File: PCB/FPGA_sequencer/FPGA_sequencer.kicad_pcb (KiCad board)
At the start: 2 copper layers, 19 parts, among them U1 ADA4940-2ACPZ-R7_a, U2 AD9648BCPZ-125, U3 DB3S406F0L, U4 DB3S406F0L

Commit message: pass capacitor add
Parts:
- added 10n1: 0.1u, Capacitors_SMD:C_0603, F.Cu at (97.8, 13.7)
- added C10: 0.1u, Capacitors_SMD:C_0603, F.Cu at (105.5, 16.1)
- added C11: 0.1u, Capacitors_SMD:C_0603, F.Cu at (109.3, 13.7)
- added C12: 0.1u, Capacitors_SMD:C_0603, F.Cu at (101.6, 20.8)
- added C13: 10n, Capacitors_SMD:C_0603, F.Cu at (105.5, 18.4)
- added C14: 10n, Capacitors_SMD:C_0603, F.Cu at (109.3, 16.1)
- added C15: 10n, Capacitors_SMD:C_0603, F.Cu at (105.5, 20.8)
- added C3: 10u, Capacitors_SMD:C_0603, F.Cu at (97.8, 16.1)
- added C4: 10u, Capacitors_SMD:C_0603, F.Cu at (101.6, 13.7)
- added C5: 1u, Capacitors_SMD:C_0603, F.Cu at (97.8, 18.4)
- added C6: 1u, Capacitors_SMD:C_0603, F.Cu at (101.6, 16.1)
- added C7: 0.1u, Capacitors_SMD:C_0603, F.Cu at (105.5, 13.7)
- added C8: 0.1u, Capacitors_SMD:C_0603, F.Cu at (97.8, 20.8)
- added C9: 0.1u, Capacitors_SMD:C_0603, F.Cu at (101.6, 18.4)
- C1, C2: footprint Capacitor_SMD:C_0603_1608Metric -> Capacitors_SMD:C_0603
- moved U2 9.48 mm to (134.1, 33.0)
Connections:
- U1 pad 10: Net-(U1-Pad10) -> Net-(C11-Pad2)
- U1 pad 15: Net-(U1-Pad15) -> Net-(10n1-Pad1)
- U1 pad 16: Net-(U1-Pad16) -> Net-(10n1-Pad1)
- U1 pad 22: Net-(U1-Pad22) -> Net-(10n1-Pad1)
- U1 pad 3: Net-(U1-Pad3) -> Net-(C11-Pad2)
- U1 pad 4: Net-(U1-Pad4) -> Net-(C11-Pad2)
- U1 pad 9: Net-(U1-Pad9) -> Net-(C11-Pad2)
- U1 pad HTAB: Net-(U1-PadHTAB) -> Net-(10n1-Pad1)
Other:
- board text added: "AD4049 pass cap"
- board text added: "ADC Driver part Cluster"

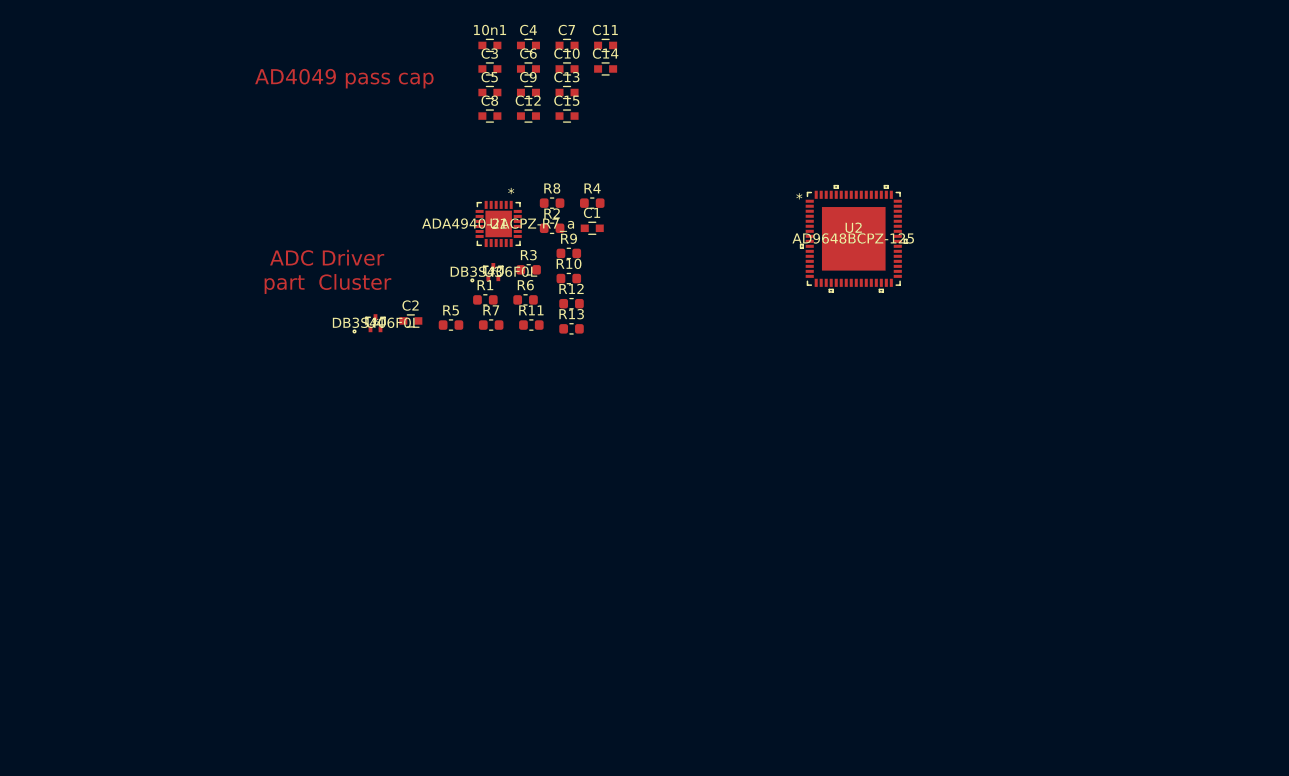
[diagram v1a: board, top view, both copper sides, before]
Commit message: MAX4565 Analog switch add
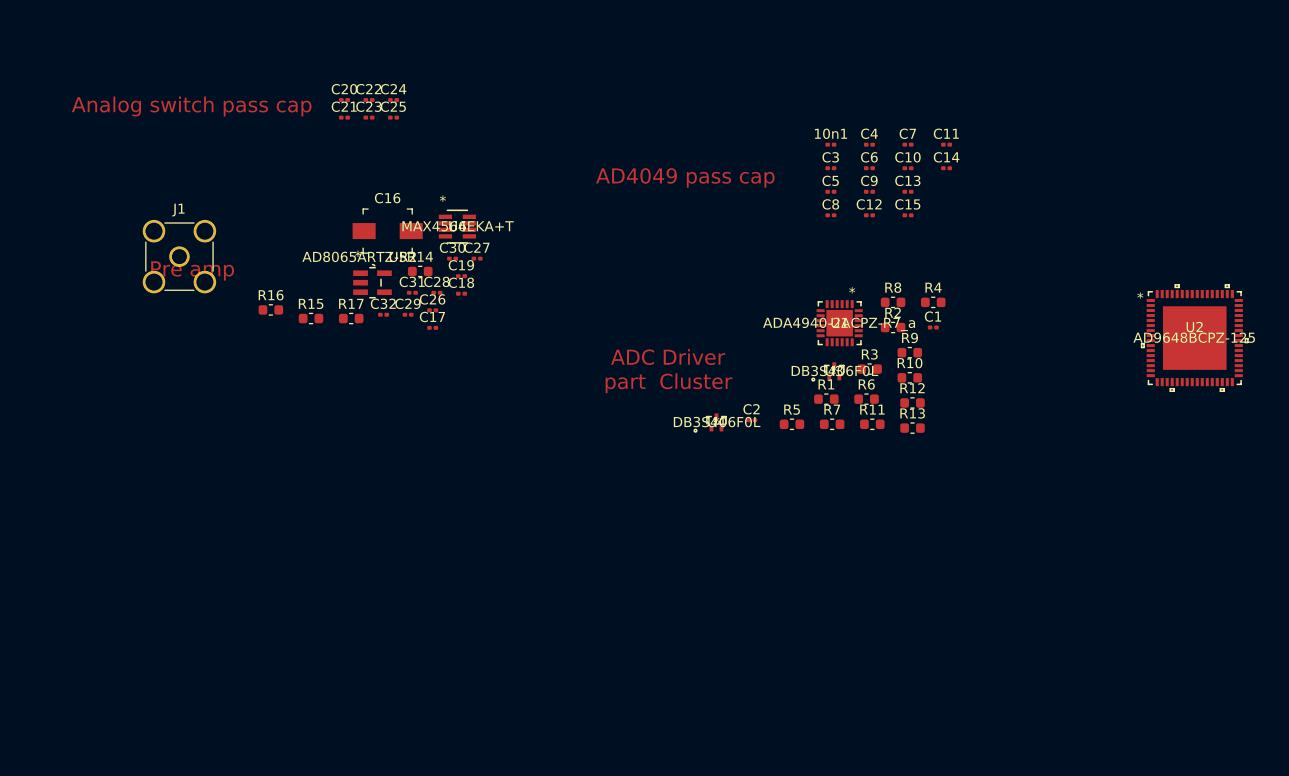
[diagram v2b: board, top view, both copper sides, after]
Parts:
- added C16: C_Variable, Capacitor_SMD:C_Trimmer_Murata_TZB4-A, F.Cu at (87.6, 32.2)
- added C17: 33p, Capacitor_SMD:C_0201_0603Metric, F.Cu at (92.1, 41.9)
- added C18: 91p, Capacitor_SMD:C_0201_0603Metric, F.Cu at (95.0, 38.5)
- added C19: 1n, Capacitor_SMD:C_0201_0603Metric, F.Cu at (95.0, 36.7)
- added C20: 10n, Capacitor_SMD:C_0201_0603Metric, F.Cu at (83.3, 19.2)
- added C21: 10n, Capacitor_SMD:C_0201_0603Metric, F.Cu at (83.3, 20.9)
- added C22: 0.1u, Capacitor_SMD:C_0201_0603Metric, F.Cu at (85.7, 19.2)
- added C23: 0.1u, Capacitor_SMD:C_0201_0603Metric, F.Cu at (85.7, 20.9)
- added C24: 1u, Capacitor_SMD:C_0201_0603Metric, F.Cu at (88.2, 19.2)
- added C25: 1u, Capacitor_SMD:C_0201_0603Metric, F.Cu at (88.2, 20.9)
- added C26: 1u, Capacitor_SMD:C_0201_0603Metric, F.Cu at (92.1, 40.2)
- added C27: 1u, Capacitor_SMD:C_0201_0603Metric, F.Cu at (96.5, 35.0)
- added C28: 0.1u, Capacitor_SMD:C_0201_0603Metric, F.Cu at (92.5, 38.4)
- added C29: 0.1u, Capacitor_SMD:C_0201_0603Metric, F.Cu at (89.6, 40.6)
- added C30: 150p, Capacitor_SMD:C_0201_0603Metric, F.Cu at (94.1, 35.0)
- added C31: 10n, Capacitor_SMD:C_0201_0603Metric, F.Cu at (90.1, 38.4)
- added C32: 10n, Capacitor_SMD:C_0201_0603Metric, F.Cu at (87.2, 40.6)
- added J1: Conn_Coaxial, Connector_Coaxial:SMA_Amphenol_132134-11_Vertical, F.Cu at (66.8, 34.8)
- added R14: 820k, Resistor_SMD:R_0603_1608Metric, F.Cu at (90.8, 36.3)
- added R15: 820k, Resistor_SMD:R_0603_1608Metric, F.Cu at (79.9, 41.0)
- added R16: 820k, Resistor_SMD:R_0603_1608Metric, F.Cu at (75.9, 40.1)
- added R17: 10k, Resistor_SMD:R_0603_1608Metric, F.Cu at (83.9, 41.0)
- added U5: AD8065ARTZ-R2, FPGA_sequencer:AD8065ARTZ-R2, F.Cu at (86.1, 37.4)
- added U6: MAX4564EKA+T, FPGA_sequencer:MAX4564EKA&plus_T, F.Cu at (94.5, 31.8)
- 10n1, C1, C10, C11, C12, C13, C14, C15, C2, C3, C4, C5, C6, C7, C8, C9: footprint Capacitors_SMD:C_0603 -> Capacitor_SMD:C_0201_0603Metric
- moved C1 35.4 mm to (142.0, 41.9)
- moved C10 35.4 mm to (139.5, 26.0)
- moved C13 35.4 mm to (139.5, 28.3)
- moved C15 35.4 mm to (139.5, 30.7)
- moved C7 35.4 mm to (139.5, 23.6)
- moved R10 35.4 mm to (139.7, 46.9)
- moved R7 35.4 mm to (132.0, 51.5)
- moved R9 35.4 mm to (139.7, 44.4)
- moved U1 35.4 mm to (132.7, 41.4)
- moved R4 35.4 mm to (142.0, 39.4)
- moved C11 35.4 mm to (143.4, 23.6)
- moved C14 35.4 mm to (143.4, 26.0)
- moved C2 35.4 mm to (123.9, 51.1)
- moved R1 35.4 mm to (131.4, 49.0)
- moved R11 35.4 mm to (136.0, 51.5)
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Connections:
- net Net-(10n1-Pad1) renamed -3V3
- net Net-(C11-Pad2) renamed +3V3
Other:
- board text added: "Analog switch pass cap"
- board text added: "Pre amp"

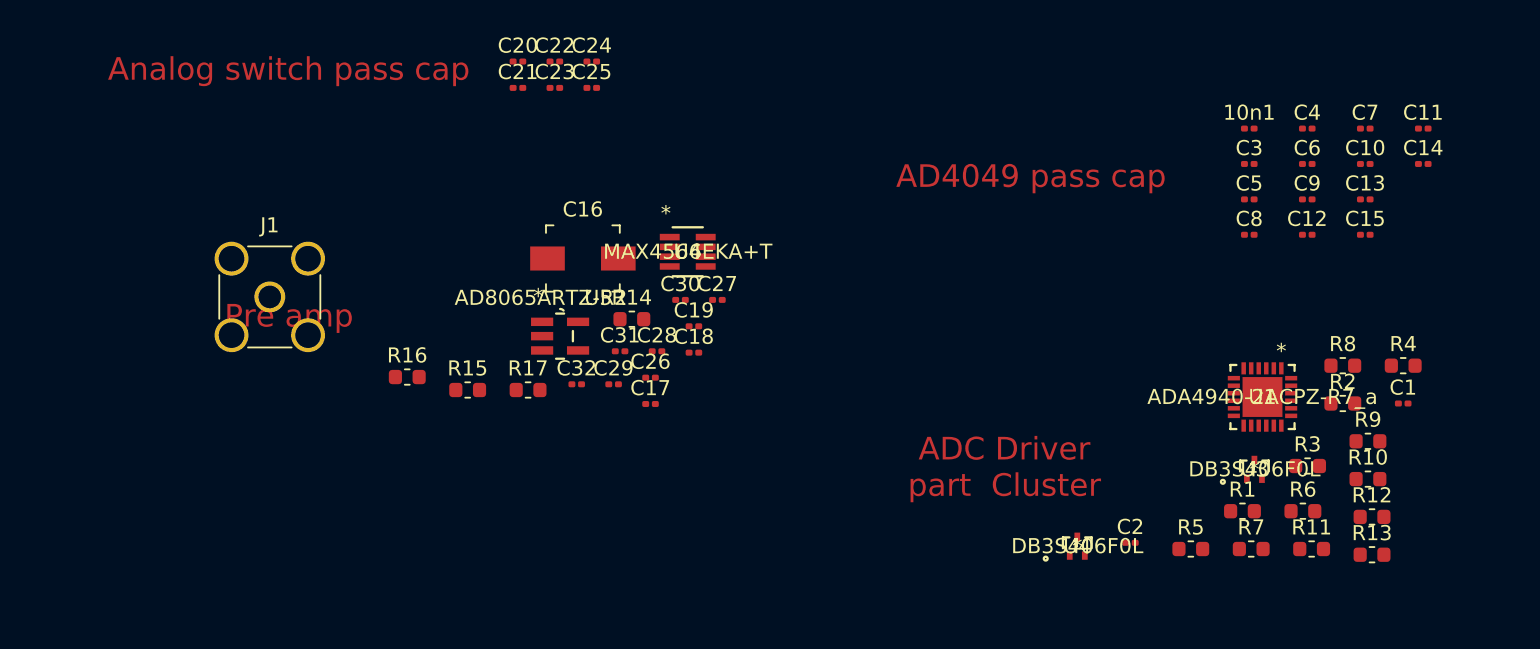
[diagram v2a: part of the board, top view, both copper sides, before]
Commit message: ADC driver pattern write
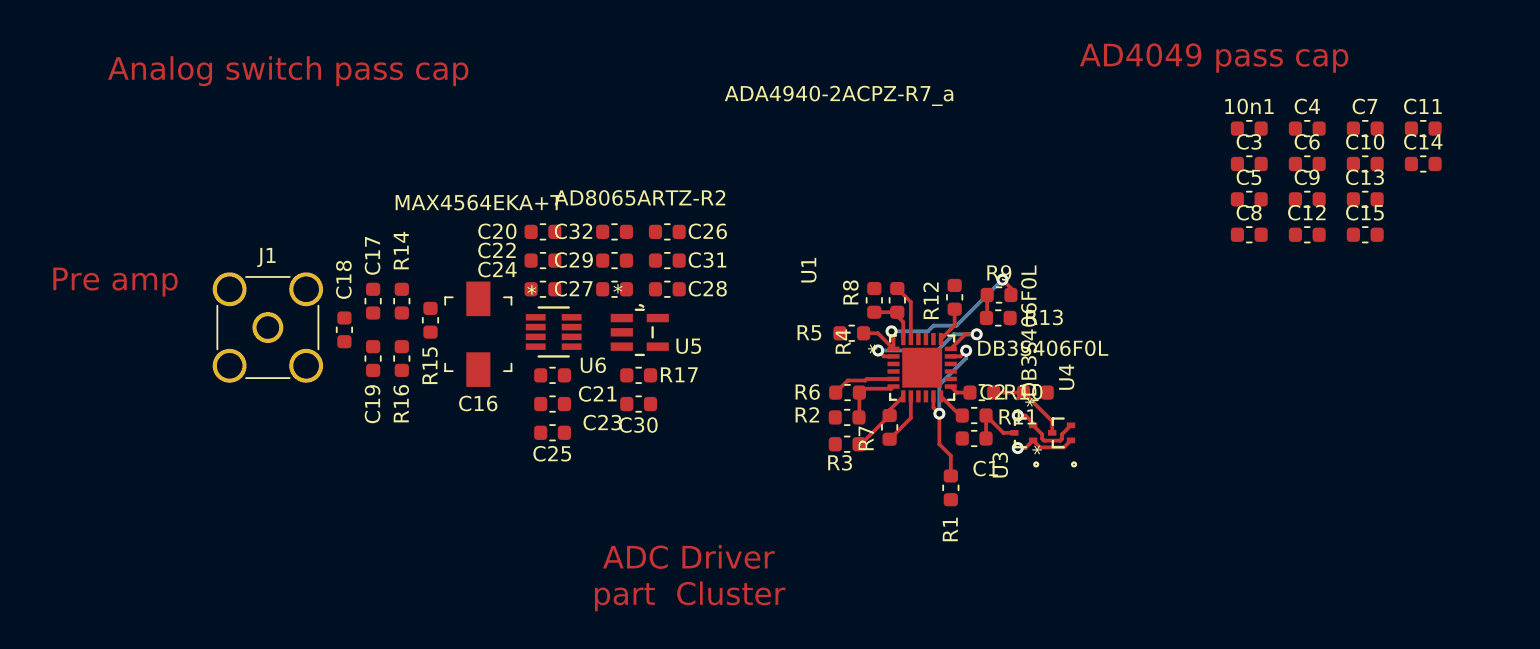
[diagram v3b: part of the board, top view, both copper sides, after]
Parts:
- 10n1, C1, C10, C11, C12, C13, C14, C15, C17, C18, C19, C2, C20, C21, C22, C23, C24, C25, C26, C27, C28, C29, C3, C30, C31, C32, C4, C5, C6, C7, C8, C9: footprint Capacitor_SMD:C_0201_0603Metric -> Capacitor_SMD:C_0603_1608Metric
- moved R4 35.4 mm to (106.9, 35.0), turned to 90 degrees
- moved R2 32.9 mm to (105.1, 42.8), turned to 180 degrees
- moved R12 31.3 mm to (112.3, 34.8), turned to 270 degrees
- moved R6 31.2 mm to (105.2, 41.1)
- moved R3 30.6 mm to (105.1, 44.6)
- moved R8 29.9 mm to (108.5, 35.0), turned to 270 degrees
- moved R13 29.4 mm to (115.2, 36.2), turned to 180 degrees
- moved C1 28.6 mm to (113.6, 44.2)
- moved R5 26.7 mm to (105.4, 37.2), turned to 180 degrees
- moved R9 26.3 mm to (115.2, 34.7)
- moved R10 26.3 mm to (114.1, 41.1)
- moved R7 25.3 mm to (108.0, 43.5), turned to 90 degrees
- moved R11 24.1 mm to (113.6, 42.7), turned to 180 degrees
- moved C18 23.3 mm to (71.8, 37.0), turned to 90 degrees
- moved C25 23.0 mm to (85.6, 43.8), turned to 180 degrees
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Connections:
- C20 pad 1: Net-(C20-Pad1) -> GNDA
- C22 pad 1: Net-(C20-Pad1) -> GNDA
- C24 pad 1: Net-(C20-Pad1) -> GNDA
- U6 pad 2: Net-(C20-Pad1) -> Net-(C20-Pad2)
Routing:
- net Net-(R5-Pad1): track 0.00 -> 13.9 mm, vias 0 -> 2
- net Net-(R1-Pad1): track 0.00 -> 11.9 mm, vias 0 -> 2
- net Net-(R13-Pad2): track 0.00 -> 11.8 mm, vias 0 -> 2
- net Net-(C2-Pad1): track 0.00 -> 6.05 mm
- net Net-(R13-Pad1): track 0.00 -> 5.45 mm, vias 0 -> 1
- net Net-(R3-Pad2): track 0.00 -> 4.47 mm
- net Net-(R6-Pad1): track 0.00 -> 4.21 mm
- net Net-(R12-Pad1): track 0.00 -> 4.13 mm, vias 0 -> 1
- net Net-(R2-Pad1): track 0.00 -> 3.99 mm
- net Net-(C1-Pad2): track 0.00 -> 3.95 mm
- net Net-(R8-Pad1): track 0.00 -> 3.73 mm
- net Net-(R4-Pad1): track 0.00 -> 3.47 mm
- net Net-(R7-Pad1): track 0.00 -> 3.43 mm
- net Net-(R12-Pad2): track 0.00 -> 2.36 mm
- net Net-(R11-Pad2): track 0.00 -> 1.94 mm
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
